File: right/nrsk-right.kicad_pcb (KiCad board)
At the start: 2 copper layers, 199.6 x 133.5 mm, 147 parts, among them J1 USB-C, J2 USB-C, J3 OLED 128x32, SW1 71, SW10 8, SW11 9, SW12 0, SW13 -, SW14 =, SW15 Backspace, SW16 75, SW17 Y, SW18 U, SW19 I, SW2 F7, SW20 O, SW21 P, SW22 [, SW23 ], SW24 \, SW25 77, SW26 H, SW27 J, SW28 K, SW29 L, SW3 F8, SW30 ;, SW31 ', SW32 Enter, SW33 79, SW34 N, SW35 M, SW36 ,, SW37 ., SW38 /, SW39 ↑, SW4 F9, SW40 fn, SW41 81, SW42 Space, SW43 Space, SW44 Cmd, SW45 Opt, SW46 ←, SW47 ↓, SW48 →, SW5 F10, SW6 F11, SW7 F12, SW8 73, SW9 7, U1 RP2040, U2 USBLC6-2SC6, U4 AP2112K-3.3, U5 W25Q128JVS, Y1 12MHz

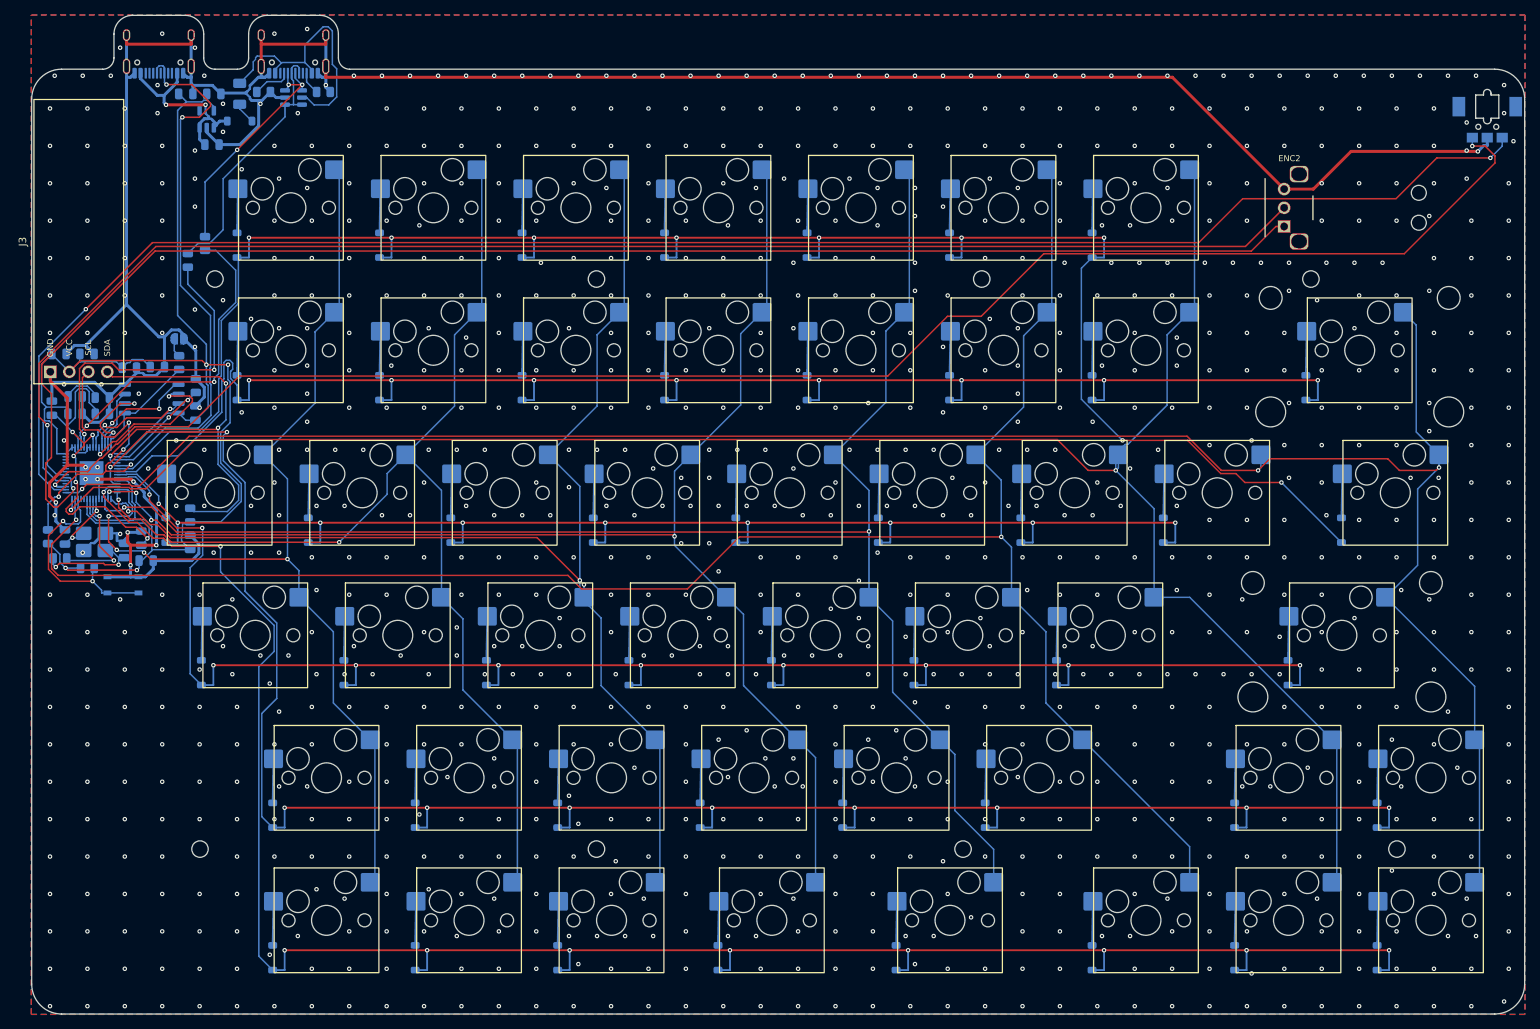
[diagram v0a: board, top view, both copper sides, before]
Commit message: Remove the blank inner key column on both halves; even plate band round the OLED cover
KLE: the unlabeled keys of the inner column go (left 8, 16, 23, 30, 37, 44; right 71, 73, 75, 77, 79, 81), so
the halves have 38 + 42 = 80 keys. The right "\" key now sits in its own row (row 2, col 7) and the remap goes;
the left's COL7 stays unconnected in the schematic.

The gap is closed: the right board moves its keys one unit in (key_shift +1 u, width -1 u). The left board is
sized from its row 0-1 keycaps: COVER_FRAME + the OLED cover (window + 5 mm each side) + COVER_FRAME, less the
case wall, so it narrows by 15.4 mm instead of a full unit.

The OLED's half-mirror cover is now laid out from the plate band round it: 3.5 mm to the case outline (top and
inner edge), to the nearest row 0-1 keycaps, and to the row-2 keycap line below, on both halves; the corner at the
case corner is concentric with it (R9), the others R2. The OLED stays at its height: its display glass, 3 mm
toward the module's top, lands at the cover's centre, and higher up the module would leave the board's rounded
corner and meet the link USB-C's shield pins. make_case checks the band against keycaps and the outline.

Sizes: boards 157.1 / 180.5 x 126.3 mm, cases 174.1 / 197.5 x 143.3 mm. The drum stays centred on Backspace.
Docs (README, ordering, pre-order checklist, drum spec coordinates) follow: 80 switches / sockets / diodes,
69 1 u keycaps, LCSC 85 switches and 90 sockets, trays fit a 220 mm bed.

Checked: ./build.sh -> left 0 unconnected (31 zero-length router stubs removed), right 0 unconnected, 0 parity
issues, ERC 0 / 0; DRC 4 silkscreen-at-board-edge warnings per side, as on main; make_case.py checks ok on both
halves (OLED band, drum dial); make_jlc: left 77, right 81 placements; textlint 0 on the edited docs.

Co-Authored-By: Claude Opus 5.5 <noreply@anthropic.com>
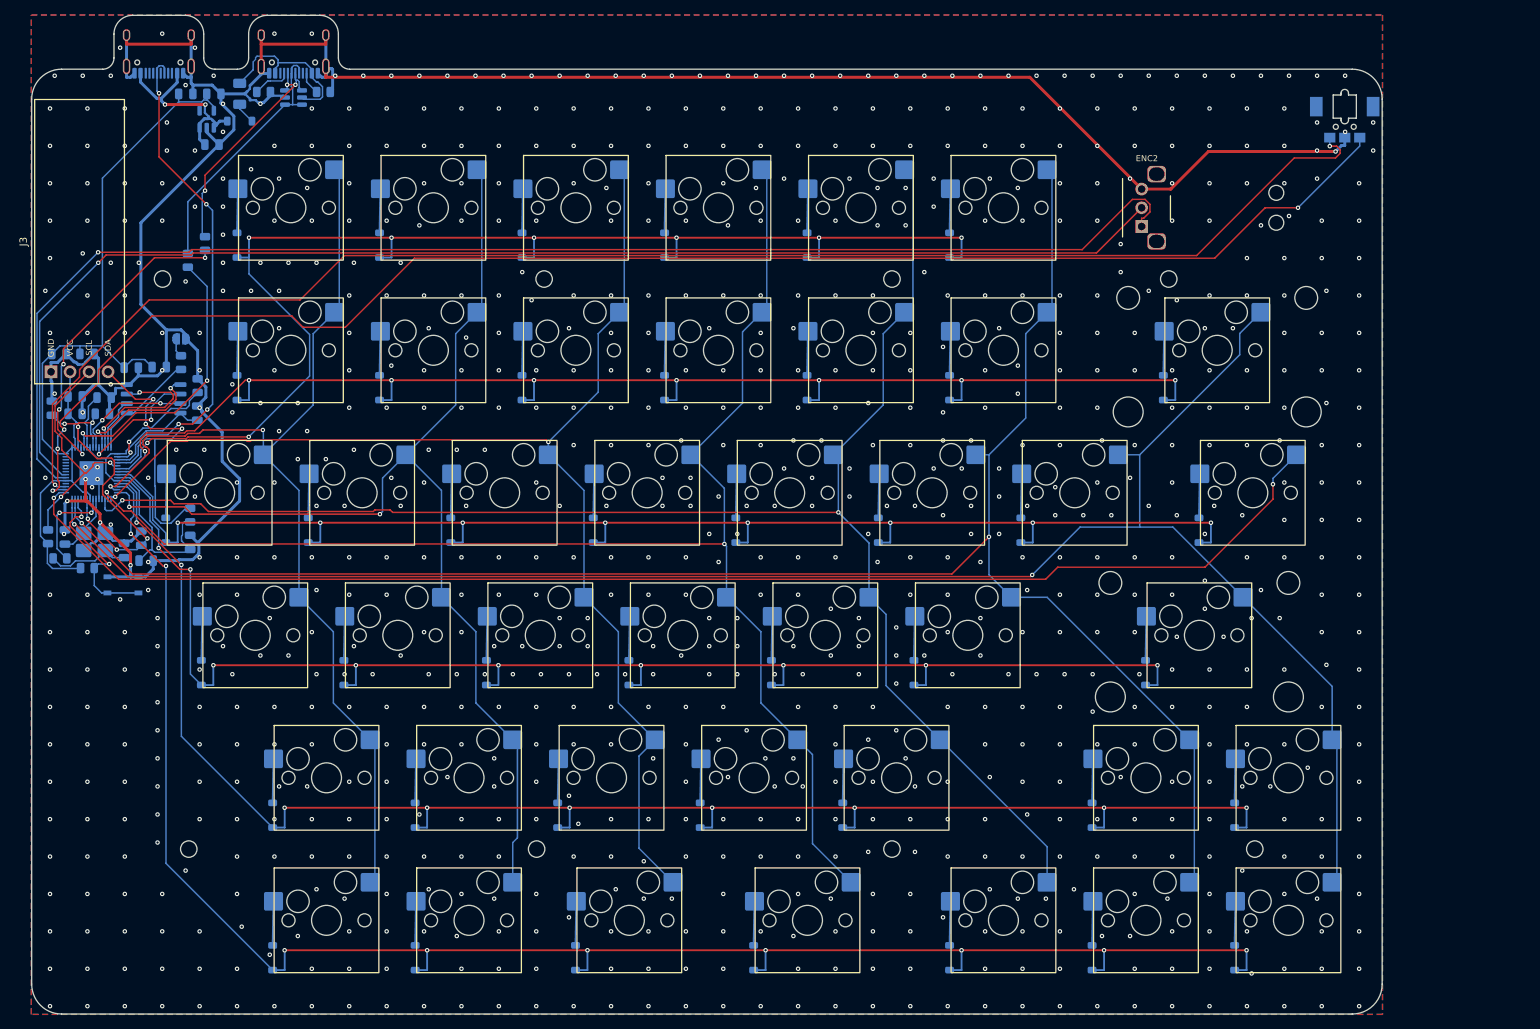
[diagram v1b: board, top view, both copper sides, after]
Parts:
- removed D43, D44, D45, D46, D47, D48: 1N4148W, Diode_SMD:D_SOD-123
- removed SW43: Space, nrsk:SW_MX_Hotswap_1.00u
- removed SW44: Cmd, nrsk:SW_MX_Hotswap_1.25u
- removed SW45: Opt, nrsk:SW_MX_Hotswap_1.25u
- removed SW46: ←, nrsk:SW_MX_Hotswap_1.00u
- removed SW47: ↓, nrsk:SW_MX_Hotswap_1.00u
- removed SW48: →, nrsk:SW_MX_Hotswap_1.00u
- SW1: value 71 -> F7
- SW10: value 8 -> 0
- SW11: value 9 -> -
- SW12: value 0 -> =
- SW13: value - -> Backspace; footprint nrsk:SW_MX_Hotswap_1.00u -> nrsk:SW_MX_Hotswap_2.00u
- SW14: value = -> Y
- SW15: value Backspace -> U; footprint nrsk:SW_MX_Hotswap_2.00u -> nrsk:SW_MX_Hotswap_1.00u
- SW16: value 75 -> I
- SW17: value Y -> O
- SW18: value U -> P
- SW19: value I -> [
- SW2: value F7 -> F8
- SW20: value O -> ]
- SW21: value P -> \; footprint nrsk:SW_MX_Hotswap_1.00u -> nrsk:SW_MX_Hotswap_1.50u
- SW22: value [ -> H
- SW23: value ] -> J
- SW24: value \ -> K; footprint nrsk:SW_MX_Hotswap_1.50u -> nrsk:SW_MX_Hotswap_1.00u
- SW25: value 77 -> L
- SW26: value H -> ;
- SW27: value J -> '
- SW28: value K -> Enter; footprint nrsk:SW_MX_Hotswap_1.00u -> nrsk:SW_MX_Hotswap_2.25u
- SW29: value L -> N
- SW3: value F8 -> F9
- SW30: value ; -> M
- SW31: value ' -> ,
- SW32: value Enter -> .; footprint nrsk:SW_MX_Hotswap_2.25u -> nrsk:SW_MX_Hotswap_1.00u
- SW33: value 79 -> /
- SW34: value N -> ↑
- SW35: value M -> fn
- SW36: value , -> Space
- SW37: value . -> Space
- SW38: value / -> Cmd; footprint nrsk:SW_MX_Hotswap_1.00u -> nrsk:SW_MX_Hotswap_1.25u
- SW39: value ↑ -> Opt; footprint nrsk:SW_MX_Hotswap_1.00u -> nrsk:SW_MX_Hotswap_1.25u
- SW4: value F9 -> F10
- SW40: value fn -> ←
- SW41: value 81 -> ↓
- SW42: value Space -> →
- SW5: value F10 -> F11
- SW6: value F11 -> F12
- SW7: value F12 -> 7
- SW8: value 73 -> 8
- SW9: value 7 -> 9
- moved SW15 134.7 mm to (71.2, 77.6)
- moved D15 134.7 mm to (64.0, 82.6)
- moved D14 125.3 mm to (44.9, 82.6)
- moved SW14 125.3 mm to (52.1, 77.6)
- moved D24 115.9 mm to (87.8, 101.7)
- moved D7 115.9 mm to (54.5, 63.6)
- moved SW24 115.9 mm to (95.0, 96.7)
- moved SW7 115.9 mm to (61.6, 58.6)
- moved D23 111.2 mm to (68.7, 101.7)
- moved SW22 111.2 mm to (56.9, 96.7)
- moved D22 111.2 mm to (49.7, 101.7)
- moved SW23 111.2 mm to (75.9, 96.7)
- moved D42 109.5 mm to (187.8, 139.8)
- moved D41 109.5 mm to (168.8, 139.8)
- moved SW41 109.5 mm to (175.9, 134.8)
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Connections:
- D14 pad 1: /ROW1 -> /ROW2
- D15 pad 1: /ROW1 -> /ROW2
- D22 pad 1: /ROW2 -> /ROW3
- D23 pad 1: /ROW2 -> /ROW3
- D24 pad 1: /ROW0 -> /ROW3
- D29 pad 1: /ROW3 -> /ROW4
- D30 pad 1: /ROW3 -> /ROW4
- D31 pad 1: /ROW3 -> /ROW4
- D32 pad 1: /ROW3 -> /ROW4
- D36 pad 1: /ROW4 -> /ROW5
- D37 pad 1: /ROW4 -> /ROW5
- D38 pad 1: /ROW4 -> /ROW5
- D39 pad 1: /ROW4 -> /ROW5
- D40 pad 1: /ROW4 -> /ROW5
- D7 pad 1: /ROW0 -> /ROW1
- SW10 pad 1: /COL2 -> /COL3
- SW11 pad 1: /COL3 -> /COL4
- SW12 pad 1: /COL4 -> /COL5
- SW13 pad 1: /COL5 -> /COL6
- SW14 pad 1: /COL6 -> /COL0
- SW15 pad 1: /COL7 -> /COL1
- SW16 pad 1: /COL0 -> /COL2
- SW17 pad 1: /COL1 -> /COL3
- SW18 pad 1: /COL2 -> /COL4
- SW19 pad 1: /COL3 -> /COL5
- SW20 pad 1: /COL4 -> /COL6
- SW21 pad 1: /COL5 -> /COL7
- SW22 pad 1: /COL6 -> /COL0
- SW23 pad 1: /COL7 -> /COL1
- SW24 pad 1: /COL7 -> /COL2
- SW25 pad 1: /COL0 -> /COL3
- SW26 pad 1: /COL1 -> /COL4
- SW27 pad 1: /COL2 -> /COL5
- SW28 pad 1: /COL3 -> /COL6
- SW29 pad 1: /COL4 -> /COL0
- SW30 pad 1: /COL5 -> /COL1
- SW31 pad 1: /COL6 -> /COL2
- SW32 pad 1: /COL7 -> /COL3
- SW33 pad 1: /COL0 -> /COL4
- SW34 pad 1: /COL1 -> /COL5
- SW35 pad 1: /COL2 -> /COL6
- SW36 pad 1: /COL3 -> /COL0
- SW37 pad 1: /COL4 -> /COL1
- SW38 pad 1: /COL5 -> /COL2
- SW39 pad 1: /COL6 -> /COL3
- SW40 pad 1: /COL7 -> /COL4
- SW41 pad 1: /COL0 -> /COL5
- SW42 pad 1: /COL1 -> /COL6
- SW7 pad 1: /COL6 -> /COL0
- SW8 pad 1: /COL0 -> /COL1
- SW9 pad 1: /COL1 -> /COL2
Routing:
- net /COL7: track 279.1 -> 182.3 mm, vias 3 -> 2
- net /ROW0: track 244.8 -> 171.4 mm, vias 9 -> 8
- net /3V3: track 225.7 -> 173.6 mm, vias 4 -> 0
- net /ROW4: track 259.5 -> 213.9 mm, vias 10 -> 9
- net GND: track 434.1 -> 399.6 mm, vias 986 -> 879
- net /ROW5: track 264.0 -> 232.9 mm, vias 10 -> 9
- net /ROW1: track 207.8 -> 178.5 mm
- net /ROW3: track 216.6 -> 190.1 mm, vias 10 -> 9
- net /ENC_A: track 228.6 -> 204.7 mm, vias 2 -> 4
- net /DRUM_A: track 200.1 -> 183.3 mm
- net /ENC_B: track 218.8 -> 202.3 mm
- net /DRUM_B: track 192.1 -> 175.8 mm
- net /VBUS: track 36.7 -> 21.8 mm
- net /SDA: track 58.6 -> 44.0 mm
- net /COL6: track 264.6 -> 251.1 mm
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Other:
- board size 199.6 x 133.5 mm -> 180.5 x 133.5 mm

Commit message: OLED cover: 5.5 mm plate band, R7 on all four corners, display centred
The half-mirror cover now has the same R7 on all four corners. The corner facing the case corner stays
concentric with the case outline (R12.5 - band), so the band keeps its width round it; that sets the band to
5.5 mm (top, inner edge, row 0-1 keycaps), up from 3.5. The left board and case widen by 4 mm; the right
board keeps its size (its cover sits in the notch above the Y key).

The cover's bottom is no longer set by the row-2 keycap line: it runs 1.5 mm past the module's header end
(COVER_END), and the OLED sits where its display glass (3 mm toward the module's top) is the cover's centre
(OLED_Y 14.95). On the right the band down to the Y keycap is therefore 2.7 mm; make_case checks the band
beside the cover (5.5) and below it (COVER_BELOW, 2.5) separately. Perimeter screws within the band + 2 mm
of the cover go, so no screw head sits next to the rounded corner (10 case screws per side).

Sizes: boards 161.1 / 180.5 x 126.3 mm, cases 178.1 / 197.5 x 143.3 mm. README describes the cover; renders
and the A / B sheet are redone (1200 px).

Checked: ./build.sh -> left 0 unconnected (one 1.2 mm DATA stub and 47 zero-length router stubs removed),
right 0 unconnected, 0 parity issues, ERC 0 / 0, DRC 4 silkscreen-at-board-edge warnings per side as on
main; make_case.py checks ok on both halves (band, drum dial); make_jlc left 77 / right 81; textlint 0.

Co-Authored-By: Claude Opus 5.5 <noreply@anthropic.com>
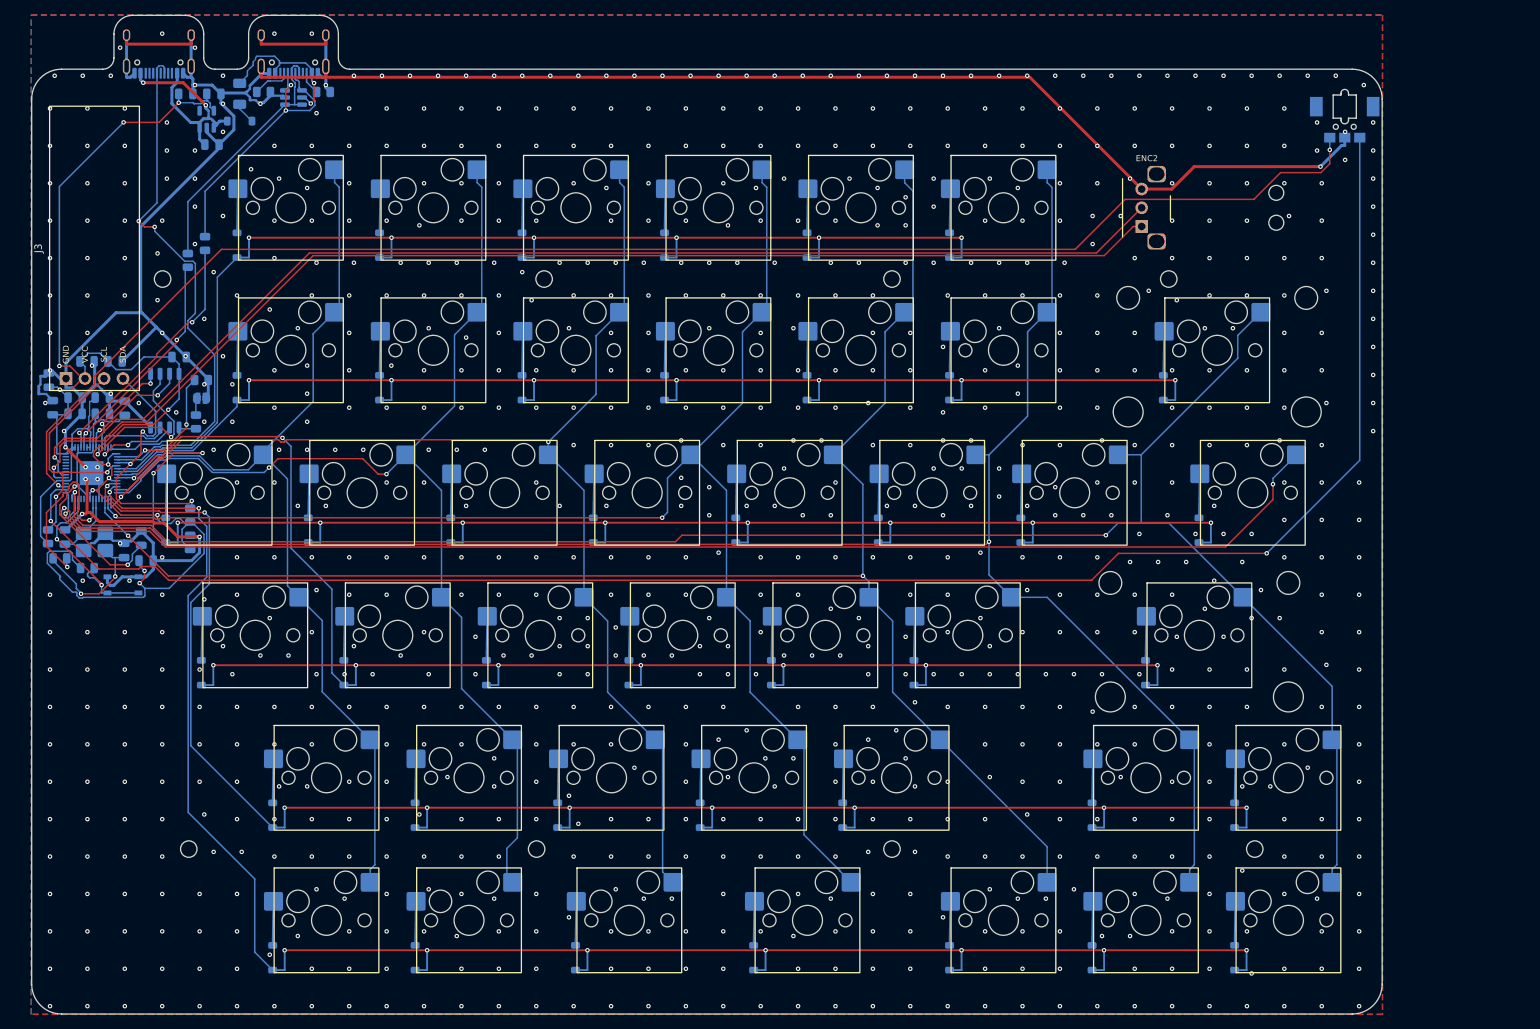
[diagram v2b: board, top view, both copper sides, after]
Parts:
- moved C14 14.9 mm to (29.3, 62.6), turned to 90 degrees
- moved C6 9.75 mm to (39.5, 66.3)
- moved C13 8.50 mm to (32.8, 64.9)
- moved JP1 8.39 mm to (49.7, 65.0)
- moved R7 8.18 mm to (49.0, 68.2)
- moved C20 7.88 mm to (46.7, 59.5), turned to 0 degrees
- moved C18 7.57 mm to (38.1, 60.1)
- moved C12 3.35 mm to (29.8, 66.2), turned to 90 degrees
- moved J3 2.19 mm to (35.4, 45.0)
- moved U5 1.52 mm to (44.8, 65.3), turned to 90 degrees
- moved C15 1.00 mm to (34.4, 60.1)
- moved R1 0.90 mm to (49.7, 62.5), turned to 0 degrees
- moved C7 0.25 mm to (36.4, 64.9)
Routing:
- net /3V3: track 173.6 -> 216.9 mm, vias 0 -> 11
- net /ENC_A: track 204.7 -> 234.1 mm, vias 4 -> 2
- net /ROW3: track 190.1 -> 216.9 mm
- net /DRUM_A: track 183.3 -> 162.8 mm
- net /ROW2: track 184.9 -> 202.4 mm, vias 8 -> 10
- net /DRUM_B: track 175.8 -> 163.1 mm
- net /XOUT: track 13.0 -> 25.2 mm
- net /ROW0: track 171.4 -> 159.8 mm, vias 8 -> 6
- net /QSPI_SD2: track 20.5 -> 9.95 mm, vias 2 -> 0
- net /ROW4: track 213.9 -> 223.3 mm
- net /1V1: track 48.6 -> 39.4 mm, vias 6 -> 2
- net /SDA: track 44.0 -> 35.1 mm
- net /D+: track 38.0 -> 29.8 mm
- net /ROW5: track 232.9 -> 240.8 mm
- net /D-: track 41.7 -> 33.8 mm, vias 4 -> 2
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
